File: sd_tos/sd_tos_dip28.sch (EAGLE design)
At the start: 20 parts, among them IC1 MEGA16-A, IC3 74HCT595D

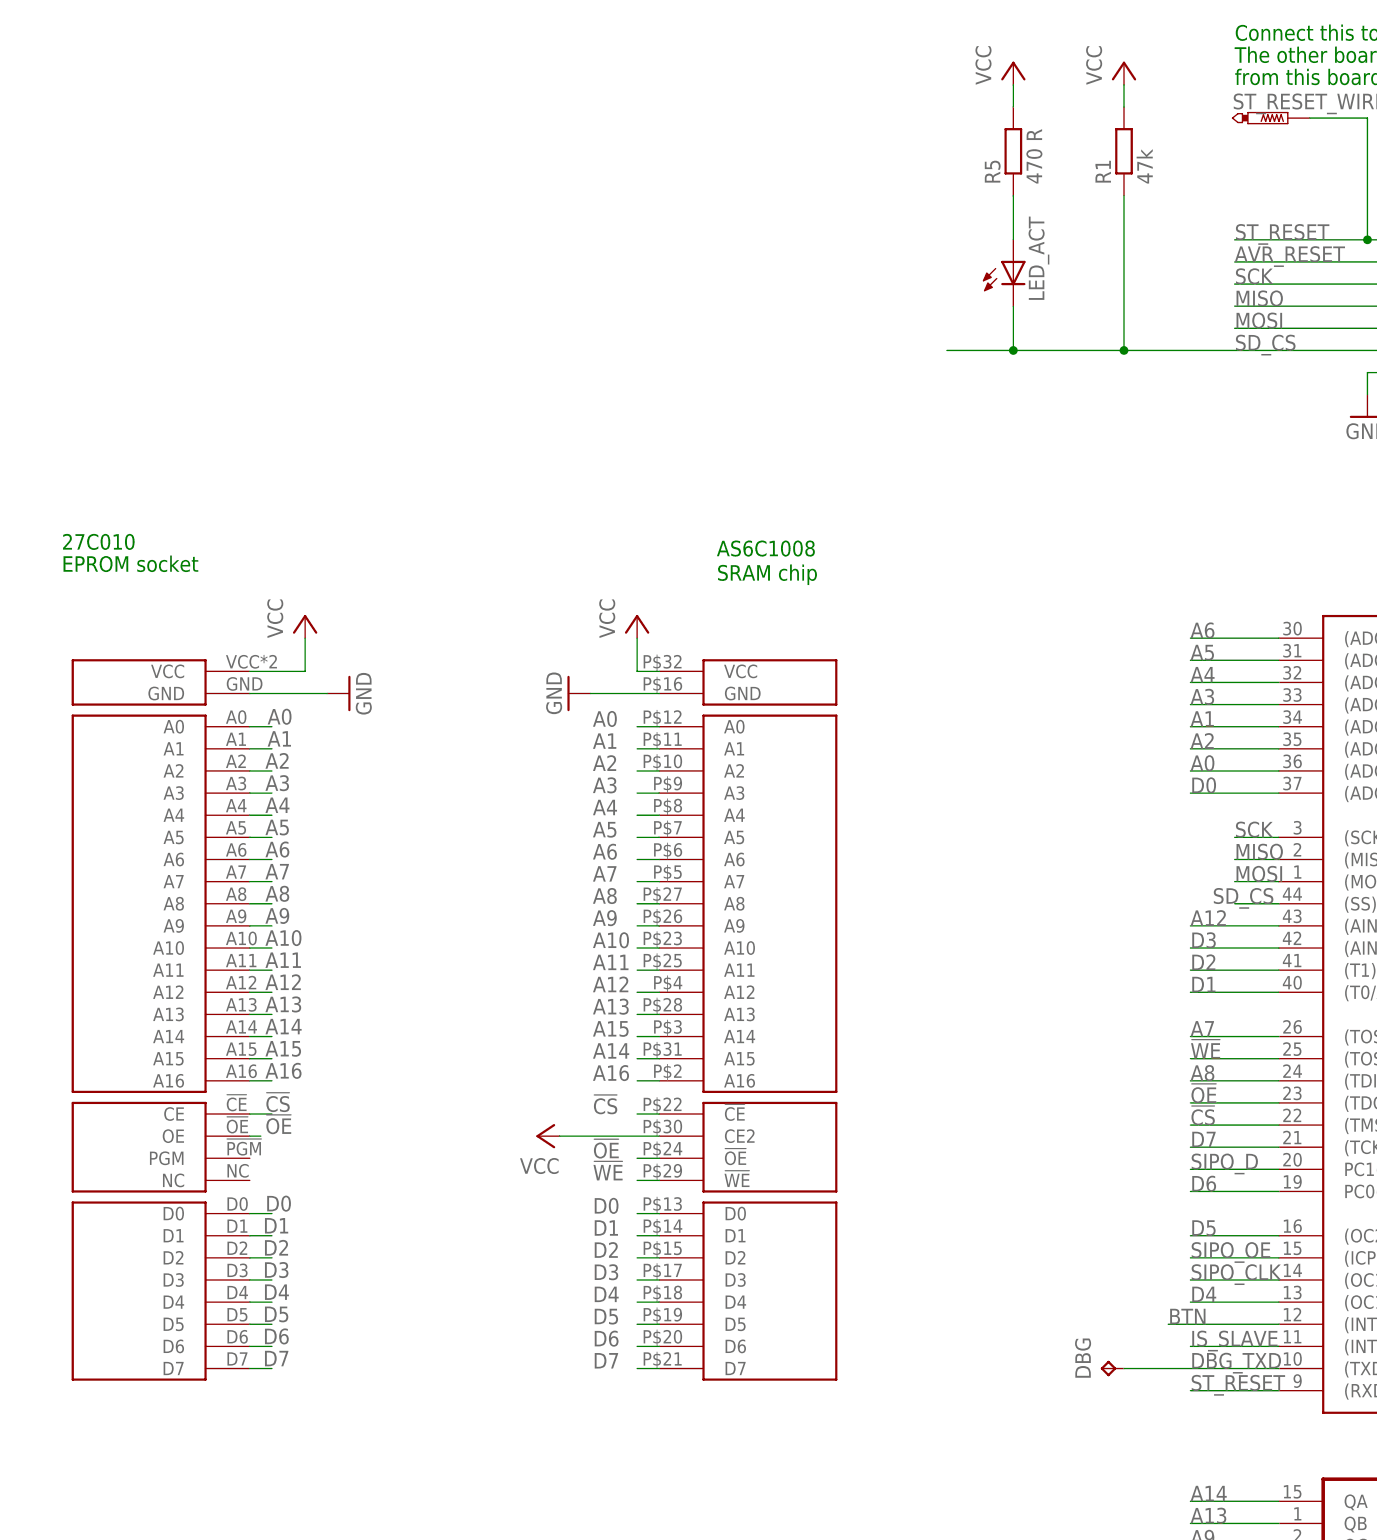
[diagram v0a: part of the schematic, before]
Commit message: added version for 28 pin EPROMs (e.g. STFM)
git-svn-id: https://subversion.assembla.com/svn/atarijookie/trunk@939 0d2ca917-fb58-4453-bb26-a698c01b0940
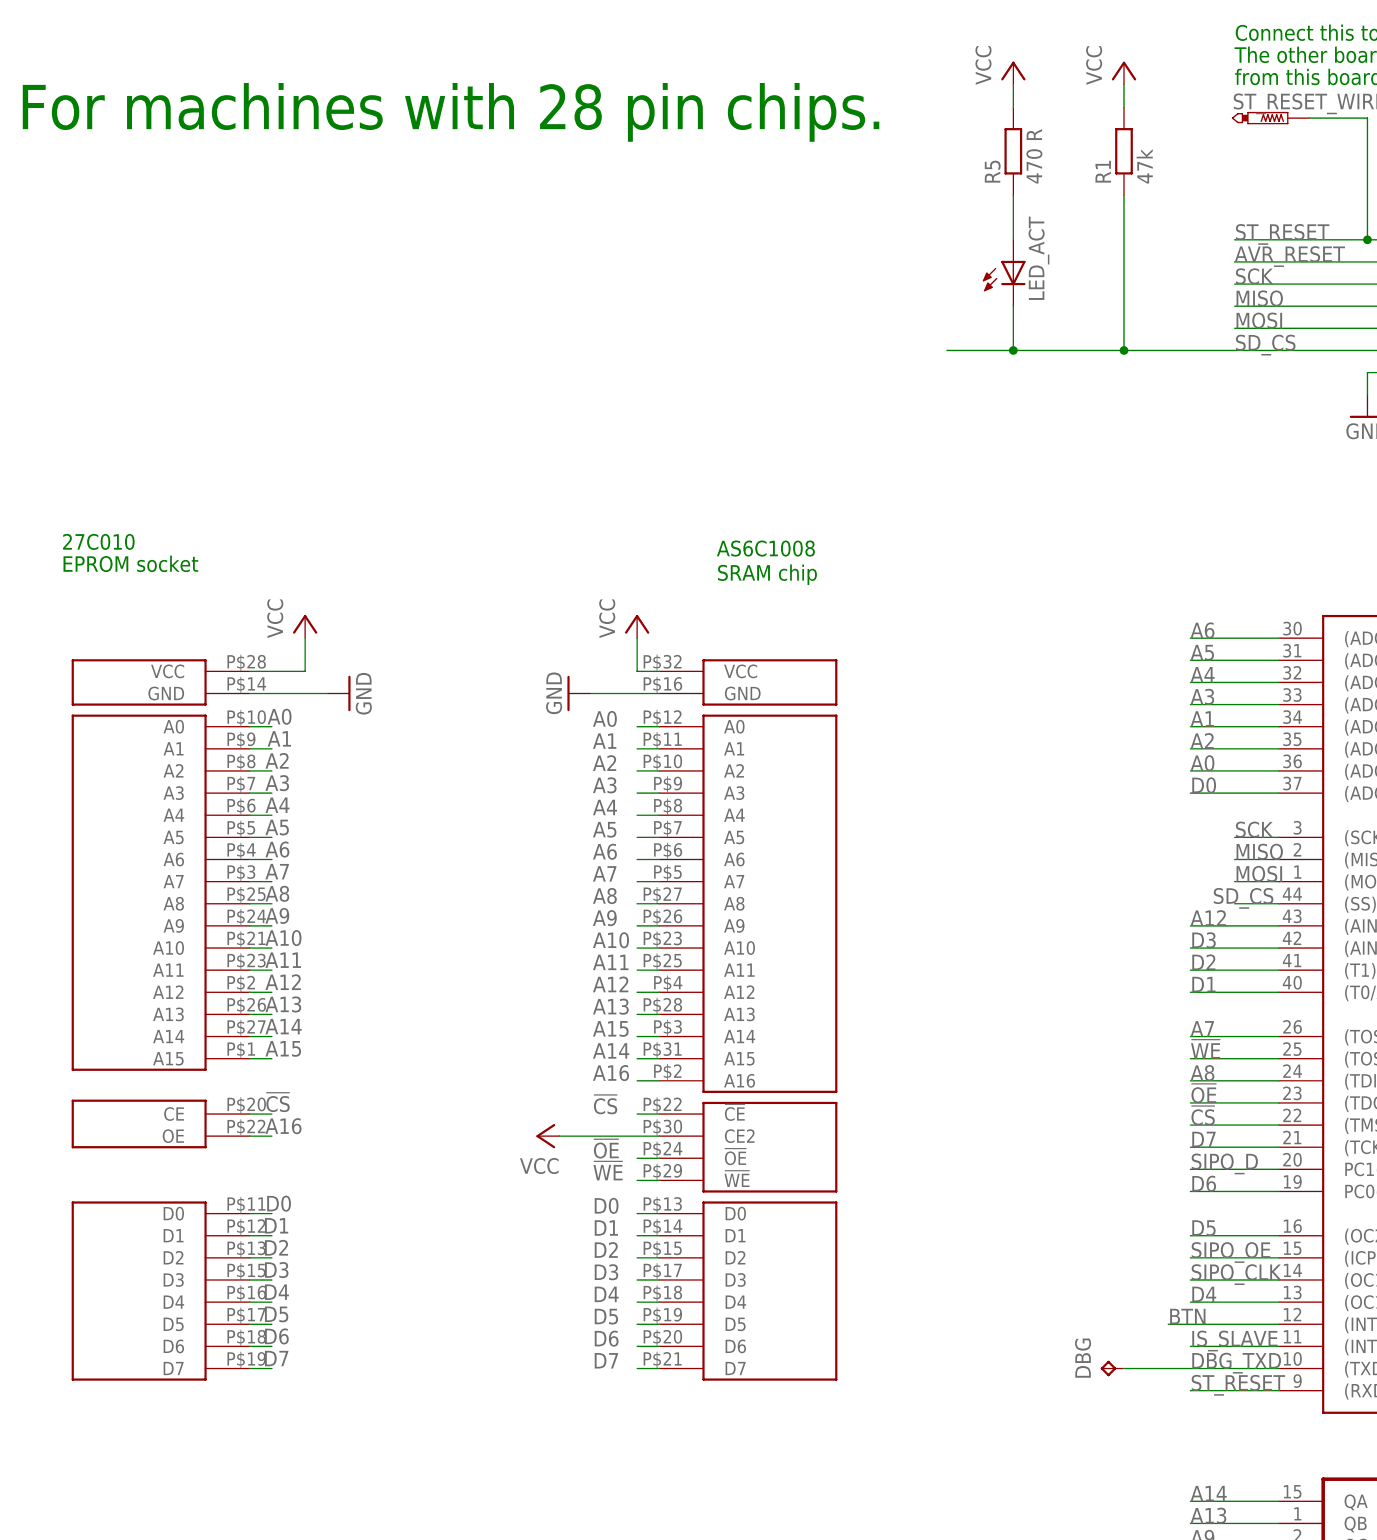
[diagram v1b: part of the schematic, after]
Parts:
- U$1: value 27C010_BOTTOM_ONLY -> 27C256BOTTOM_ONLY; device sd_tos:27C010_BOTTOM_ONLY -> sd_tos:27C256BOTTOM_ONLY
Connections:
- net !OE: no longer U$1.OE
- net A16: now also U$1.OE; no longer U$1.A16
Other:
- note added: "For machines with 28 pin chips."
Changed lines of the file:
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@@
 <part name="C3" library="rcl" deviceset="C-EU" device="C0603" value="100 nF"/>
 <part name="C5" library="rcl" deviceset="CPOL-EU" device="SANYO_SMD_B6" value="10 uF"/>
-<part name="U$1" library="sd_tos" deviceset="27C010_BOTTOM_ONLY" device=""/>
 <part name="P+1" library="supply1" deviceset="VCC" device=""/>
 <part name="P+3" library="supply1" deviceset="VCC" device=""/>
@@
 <part name="U$2" library="sd_tos" deviceset="AS6C1008" device="DIP32"/>
 <part name="DBG" library="testpad" deviceset="TP" device="B1,27"/>
+<part name="U$1" library="sd_tos" deviceset="27C256" device="BOTTOM_ONLY"/>
 </parts>
 <sheets>
@@
 <text x="137.16" y="162.56" size="1.778" layer="91">from this board through SV2 connector.</text>
 <text x="77.724" y="108.458" size="1.778" layer="91">AS6C1008</text>
+<text x="-2.54" y="157.48" size="5.08" layer="91" ratio="20">For machines with 28 pin chips.</text>
 </plain>
 <instances>
@@
 <instance part="C3" gate="G$1" x="307.34" y="40.64" rot="R180"/>
 <instance part="C5" gate="G$1" x="314.96" y="43.18"/>
-<instance part="U$1" gate="G$1" x="12.7" y="68.58" rot="MR0"/>
 <instance part="P+1" gate="VCC" x="57.15" y="41.91" rot="R90"/>
 <instance part="P+3" gate="VCC" x="30.48" y="101.6"/>
@@
 <instance part="U$2" gate="G$1" x="82.55" y="55.88"/>
 <instance part="DBG" gate="G$1" x="121.92" y="15.24" rot="R90"/>
+<instance part="U$1" gate="G$1" x="11.43" y="58.42" rot="MR0"/>
 </instances>
 <busses>
@@
 <segment>
 <wire x1="24.13" y1="95.25" x2="30.48" y2="95.25" width="0.1524" layer="91"/>
-<pinref part="U$1" gate="G$1" pin="VCC"/>
 <pinref part="P+3" gate="VCC" pin="VCC"/>
 <wire x1="30.48" y1="95.25" x2="30.48" y2="99.06" width="0.1524" layer="91"/>
+<pinref part="U$1" gate="G$1" pin="VCC"/>
 </segment>
 <segment>
@@
 <net name="A16" class="0">
 <segment>
-<wire x1="26.67" y1="48.26" x2="24.13" y2="48.26" width="0.1524" layer="91"/>
-<label x="25.908" y="48.514" size="1.778" layer="95"/>
-<pinref part="U$1" gate="G$1" pin="A16"/>
+<wire x1="26.67" y1="41.91" x2="24.13" y2="41.91" width="0.1524" layer="91"/>
+<label x="25.908" y="42.164" size="1.778" layer="95"/>
+<pinref part="U$1" gate="G$1" pin="OE"/>
 </segment>
 <segment>
@@
 </segment>
 <segment>
-<wire x1="24.13" y1="41.91" x2="25.4" y2="41.91" width="0.1524" layer="91"/>
-<label x="25.908" y="42.164" size="1.778" layer="95"/>
-<pinref part="U$1" gate="G$1" pin="OE"/>
-</segment>
-<segment>
